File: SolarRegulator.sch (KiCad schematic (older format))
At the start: 0 parts

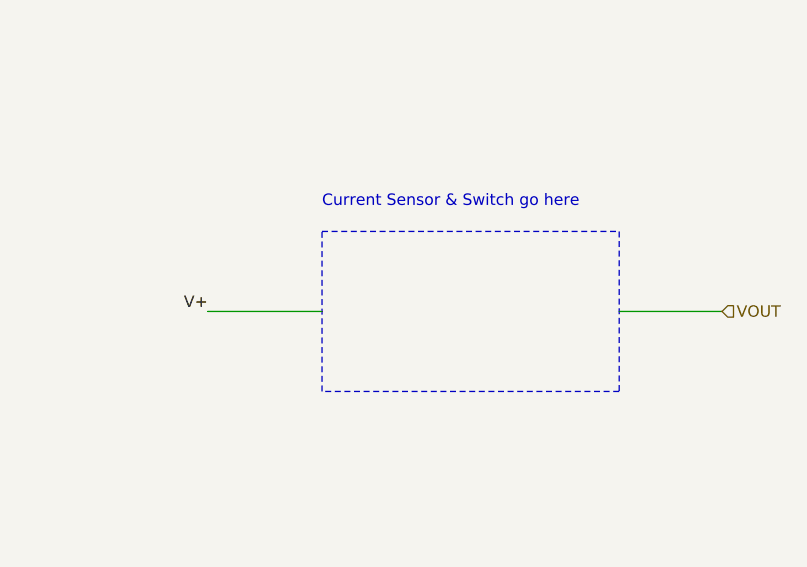
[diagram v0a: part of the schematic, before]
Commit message: moved solar cell current sensor and load switch to root sheet
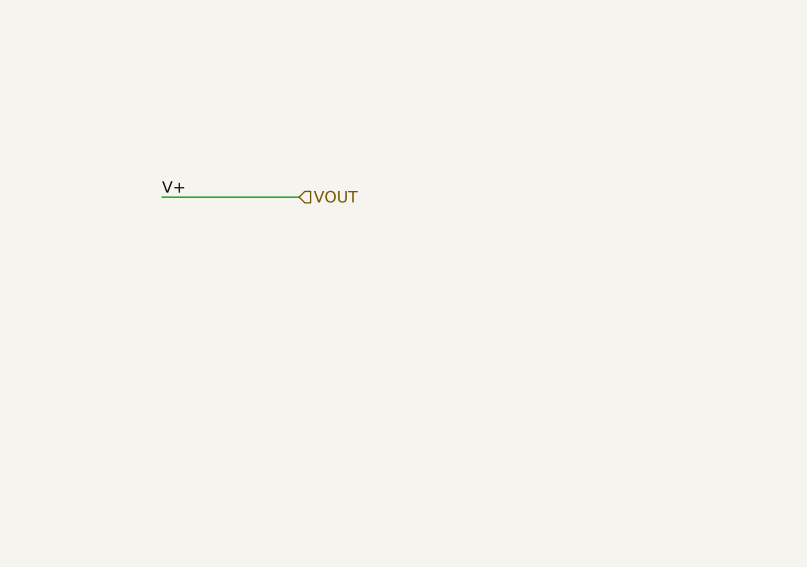
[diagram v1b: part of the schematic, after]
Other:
- note removed: "Current Sensor & Switch go here\n"
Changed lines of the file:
@@
 EESchema Schematic File Version 4
+LIBS:Main-cache
 EELAYER 29 0
 EELAYER END
@@
 Text Label 5500 7150 0    50   ~ 0
 V+
-Text Label 7300 4500 2    50   ~ 0
-V+
-Wire Notes Line
-	9100 4150 9100 4850
-Wire Notes Line
-	9100 4850 7800 4850
-Wire Notes Line
-	7800 4850 7800 4150
-Wire Notes Line
-	7800 4150 9100 4150
-Wire Wire Line
-	7300 4500 7800 4500
-Wire Wire Line
-	9100 4500 9550 4500
-Text HLabel 9550 4500 2    50   Input ~ 0
+Text Label 7100 4000 0    50   ~ 0
+V+
+Wire Wire Line
+	7100 4000 7700 4000
+Text HLabel 7700 4000 2    50   Input ~ 0
 VOUT
-Text Notes 7800 4050 0    50   ~ 0
-Current Sensor & Switch go here\n
 $EndSCHEMATC
